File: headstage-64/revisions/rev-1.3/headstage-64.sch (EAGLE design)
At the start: 195 parts, among them J8 DF40C-70DP-0.4V(51), J9 PINHD-1X5_HALF_CONNETOR, U1 ADA4062-4ACPZ-R7, U10 BNO055, U11 TS4231, U12 TS4231, U13 TLV70733, U14 10M08DC, U15 TLV70733, U16 LT3463, U17 TLV70725, U18 TPS62621, U19 ASCO-50.000MHZ-EK-T3, U2 AD5681RBCPZ-1RL7, U20 TLV70712, U3 CAT4016_QFN, U4 TPL0501_UQFN, U5 DG509B, U6 TS4231, U7 RHD2064_BGA, U8 TS4231, U9 DS90UB913A_WQFN

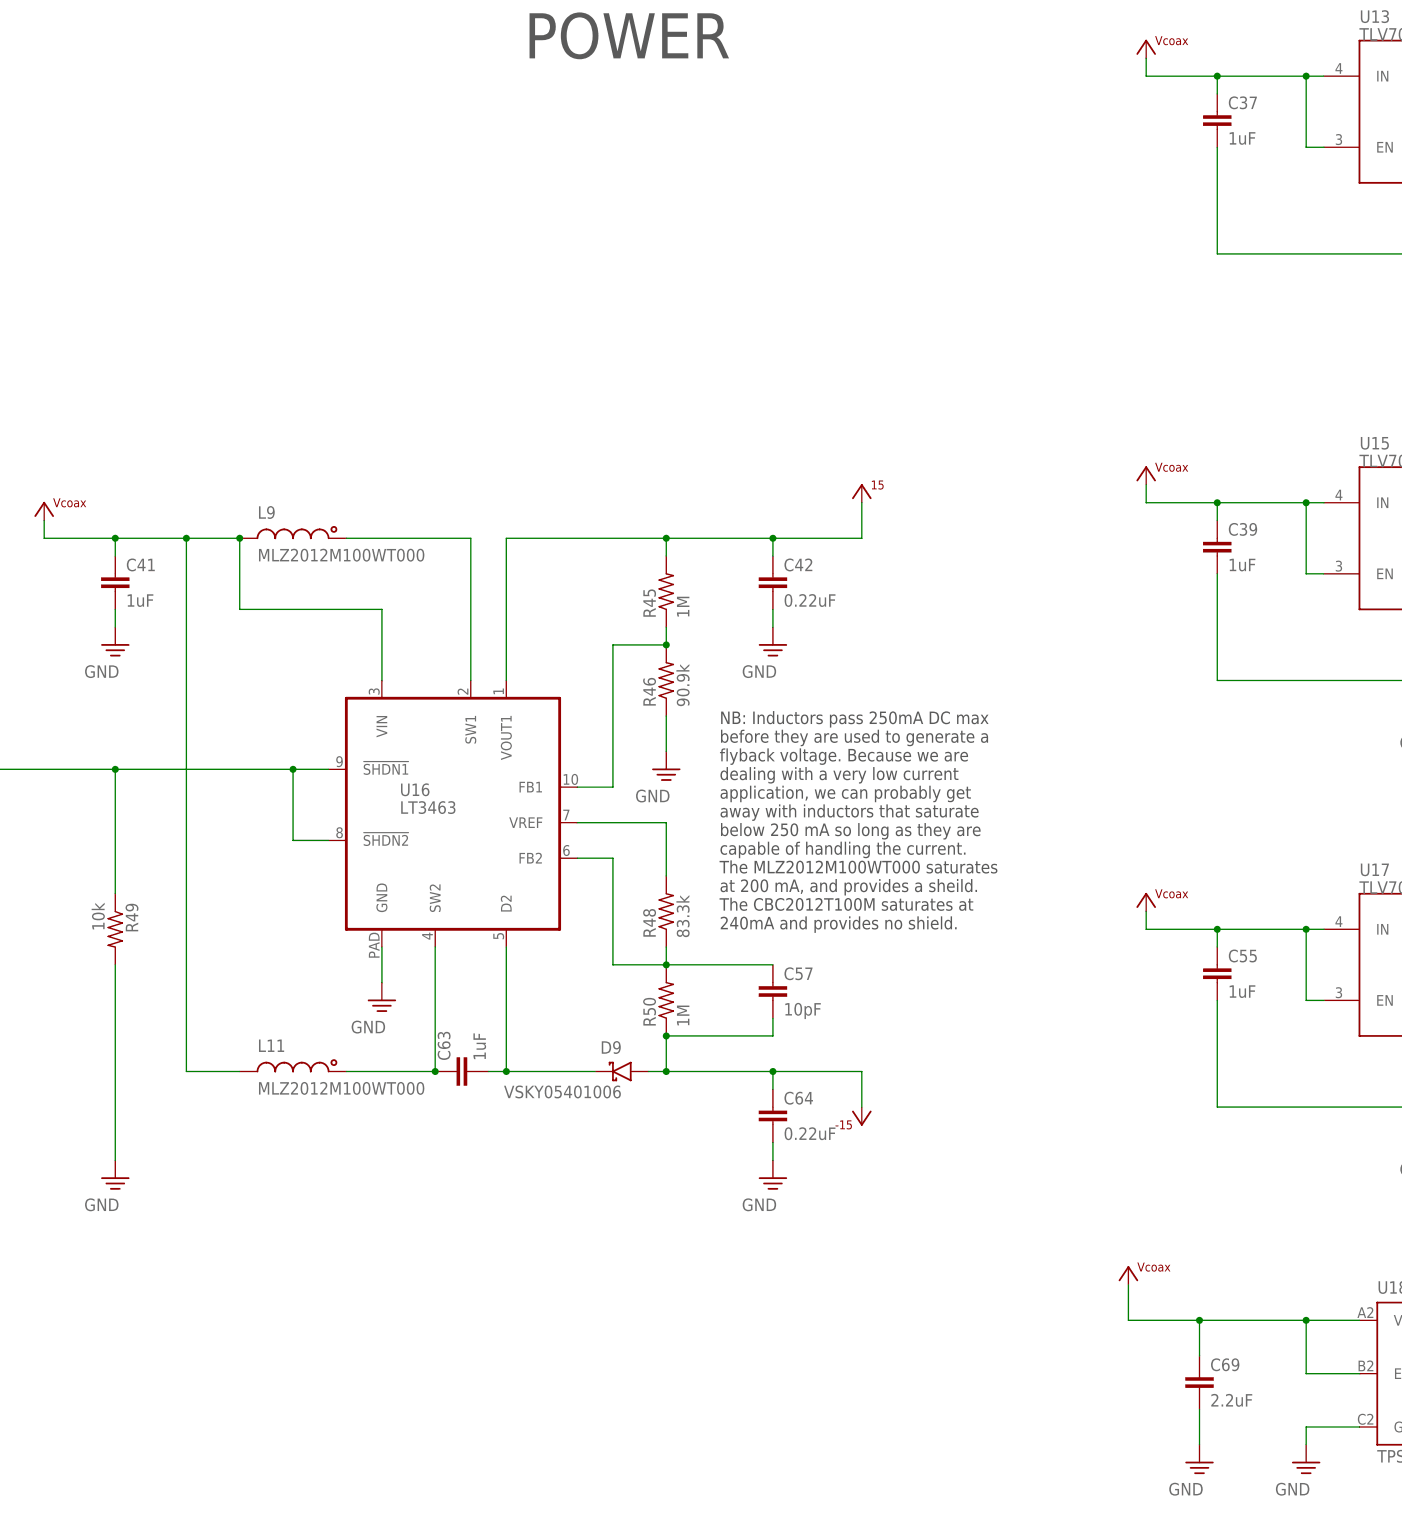
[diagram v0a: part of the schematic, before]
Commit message: Add POR pulldown to serializer on headstage-64
- Found during trouble shooting headstage-neuropix that serializer needs
a pulldown on GPIO to ensure proper POR behavior
- Also, removed silkscreen (with the exception of _tSilk and _bSilk
special layers) from the gerber files because for this design, it does
nothing but cause trouble.
- Update headstage-64 rev. 1.3 with proper decoupling capacitor values
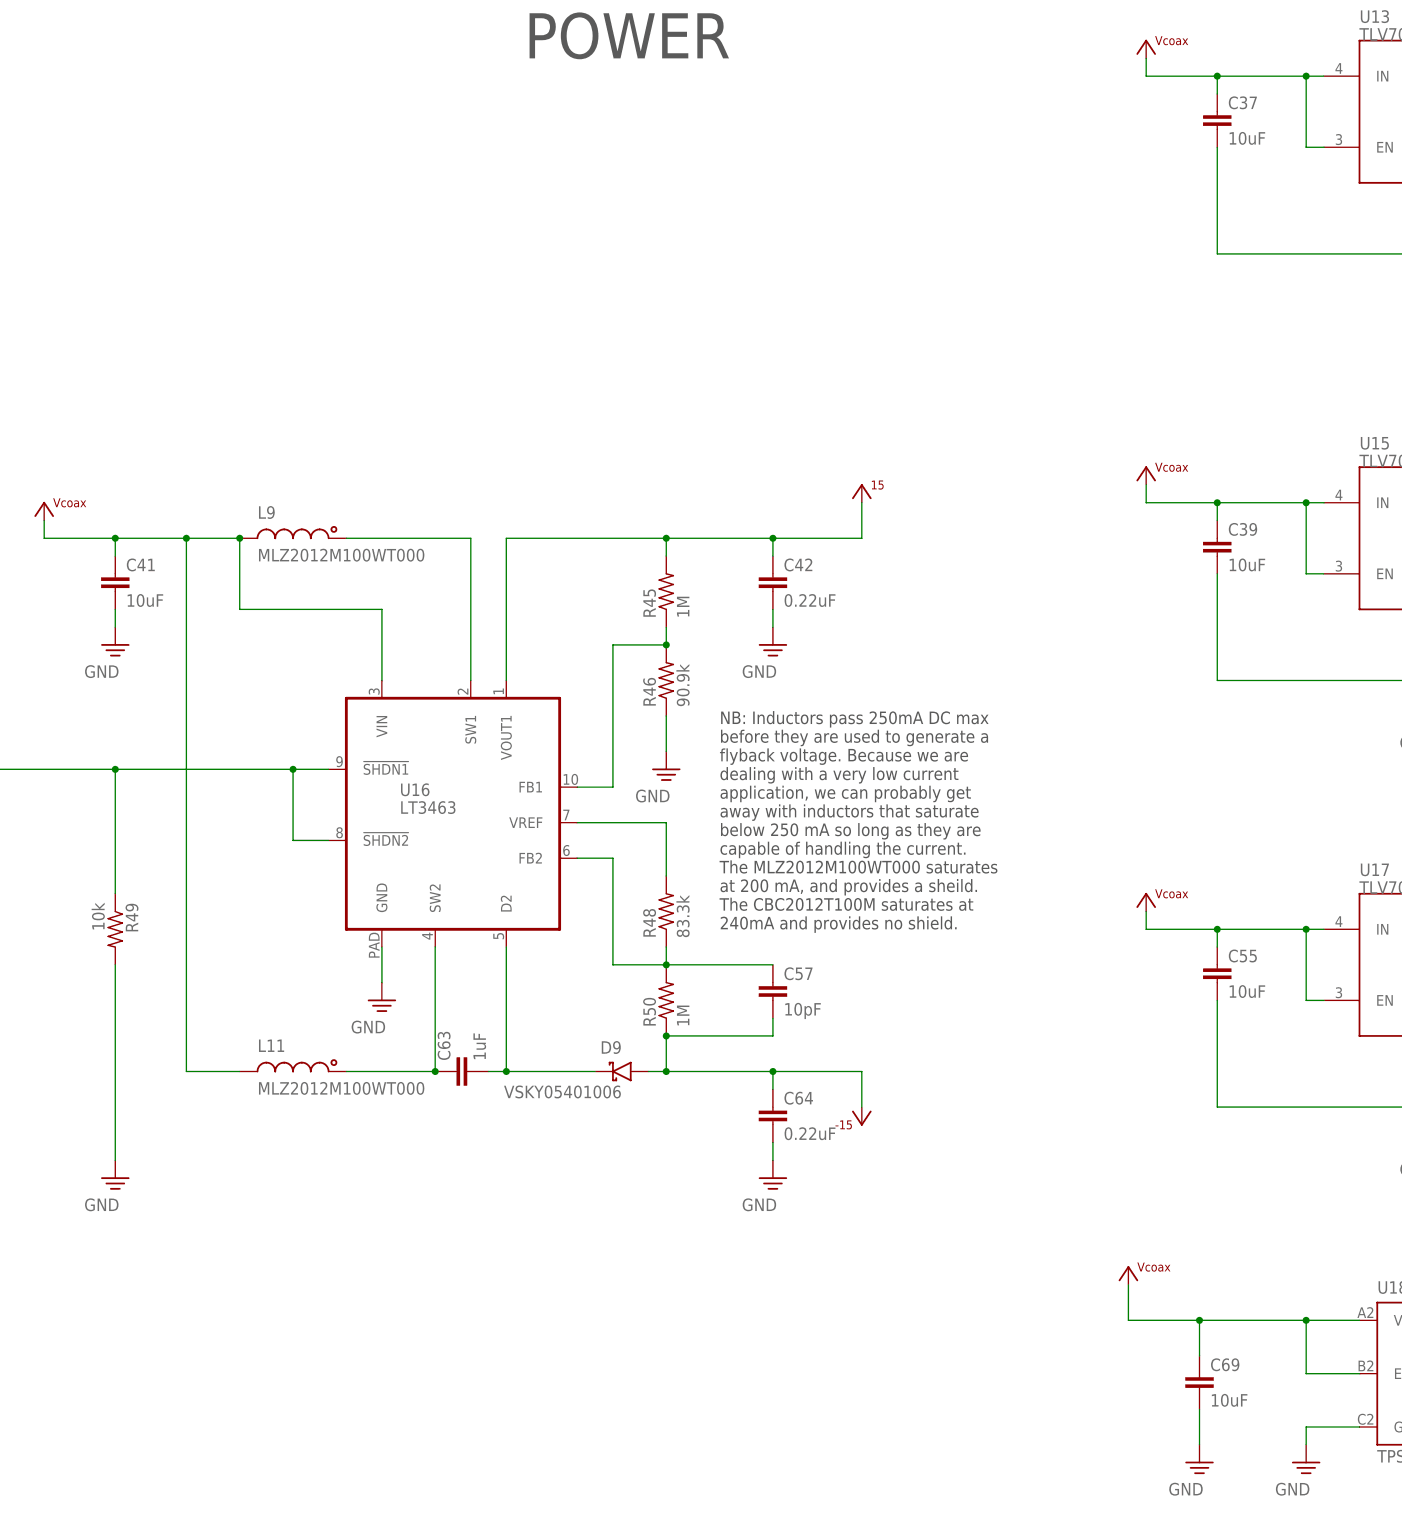
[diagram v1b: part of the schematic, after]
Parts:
- C37, C39, C41, C55: value 1uF -> 10uF
- C69: value 2.2uF -> 10uF
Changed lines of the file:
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@@
 <part name="C57" library="jonnew" deviceset="C" device="_0201T" value="10pF"/>
 <part name="SUPPLY26" library="jonnew" deviceset="GND" device=""/>
-<part name="C39" library="jonnew" deviceset="C" device="_0402T" value="1uF">
+<part name="C39" library="jonnew" deviceset="C" device="_0402T" value="10uF">
 <attribute name="PARTNO" value="CL05A105KO5NNNC"/>
 </part>
@@
 <attribute name="PARTNO" value="CL05A105KO5NNNC"/>
 </part>
-<part name="C55" library="jonnew" deviceset="C" device="_0402T" value="1uF">
-<attribute name="PARTNO" value="CL05A105KO5NNNC"/>
-</part>
-<part name="C41" library="jonnew" deviceset="C" device="_0402T" value="1uF">
+<part name="C55" library="jonnew" deviceset="C" device="_0402T" value="10uF">
+<attribute name="PARTNO" value="CL05A105KO5NNNC"/>
+</part>
+<part name="C41" library="jonnew" deviceset="C" device="_0402T" value="10uF">
 <attribute name="PARTNO" value="CL05A105KO5NNNC"/>
 </part>
@@
 <part name="SUPPLY66" library="jonnew" deviceset="AGND" device=""/>
 <part name="U13" library="jonnew" deviceset="TLV707" device="" value="TLV70733"/>
-<part name="C37" library="jonnew" deviceset="C" device="_0402T" value="1uF">
+<part name="C37" library="jonnew" deviceset="C" device="_0402T" value="10uF">
 <attribute name="PARTNO" value="CL05A105KO5NNNC"/>
 </part>
@@
 <part name="R44" library="jonnew" deviceset="R" device="_0201T" value="4.7k"/>
 <part name="U18" library="jonnew" deviceset="TPS6262X" device="" value="TPS62621"/>
-<part name="C69" library="jonnew" deviceset="C" device="_0402T" value="2.2uF">
-<attribute name="PARTNO" value="CL05A105KO5NNNC"/>
-</part>
+<part name="C69" library="jonnew" deviceset="C" device="_0402T" value="10uF">
+<attribute name="PARTNO" value="CL05A105KO5NNNC"/>
+</part>
